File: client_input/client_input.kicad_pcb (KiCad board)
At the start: 2 copper layers, 46.5 x 47.8 mm, 26 parts, among them P1 Analog In 7-0, P2 Analog In 15-8, P4 FTDI, P5 LiPo, P6 i/o 0-7, P7 i/o 9-15, P8 i/o 15-23, P9 i/o 24-31, SW1 RST, SW2 PAIR, SW3 BTLD, U1 MCP3208, U2 MCP3208, U3 ESP-12E, U4 MCP1700-3302, U5 MCP23017, U6 MCP23017

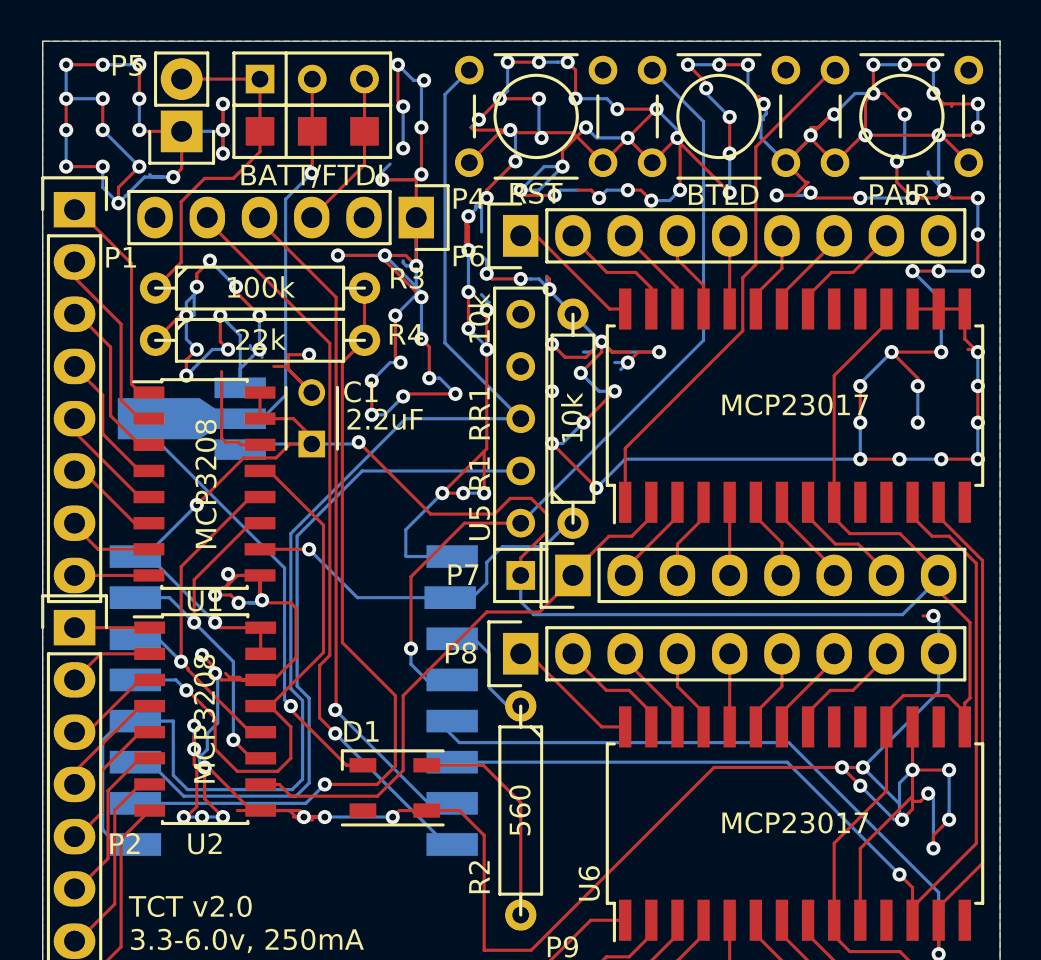
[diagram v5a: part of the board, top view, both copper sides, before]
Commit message: Nearly ready to go 2 sided. ESP + reg on back, rest on front. Stitched ground planes. Needs: some ground plane gaps filled, add some caps.
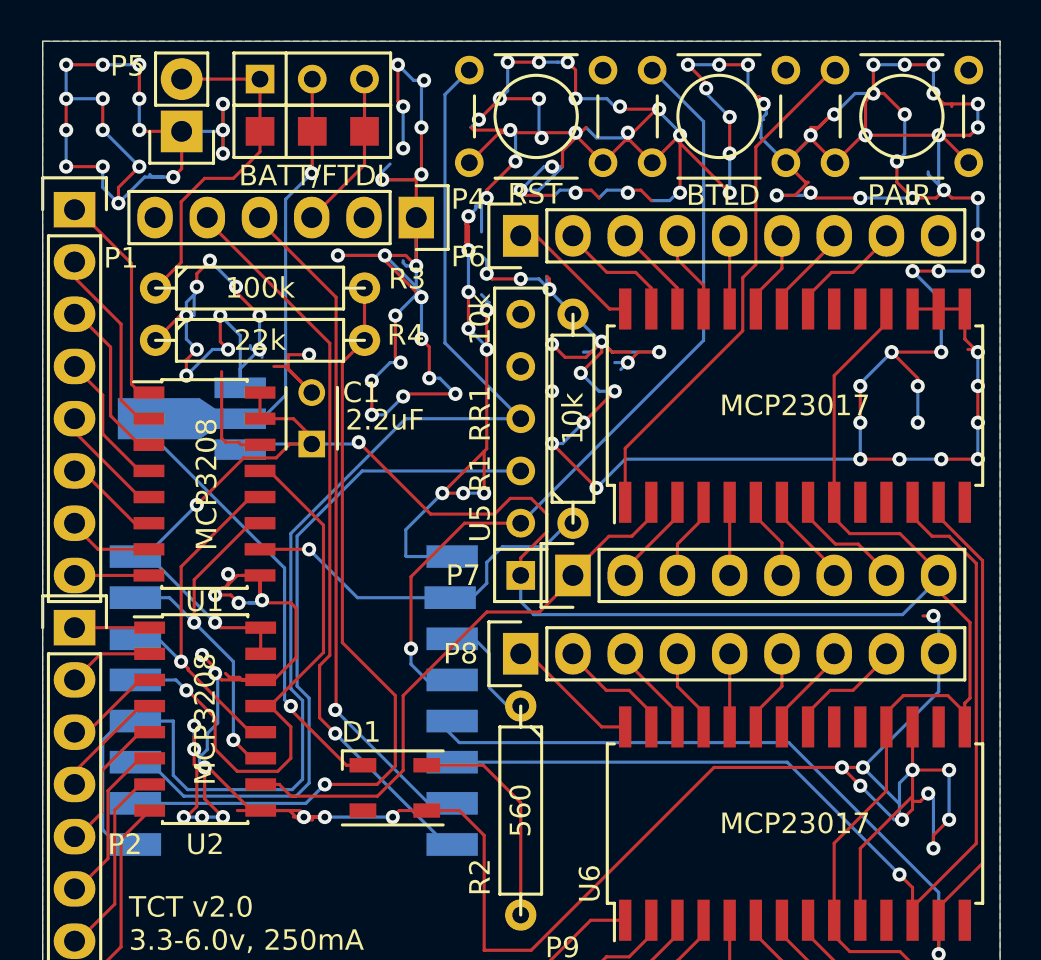
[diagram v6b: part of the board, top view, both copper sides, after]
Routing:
- net GND: vias 161 -> 159

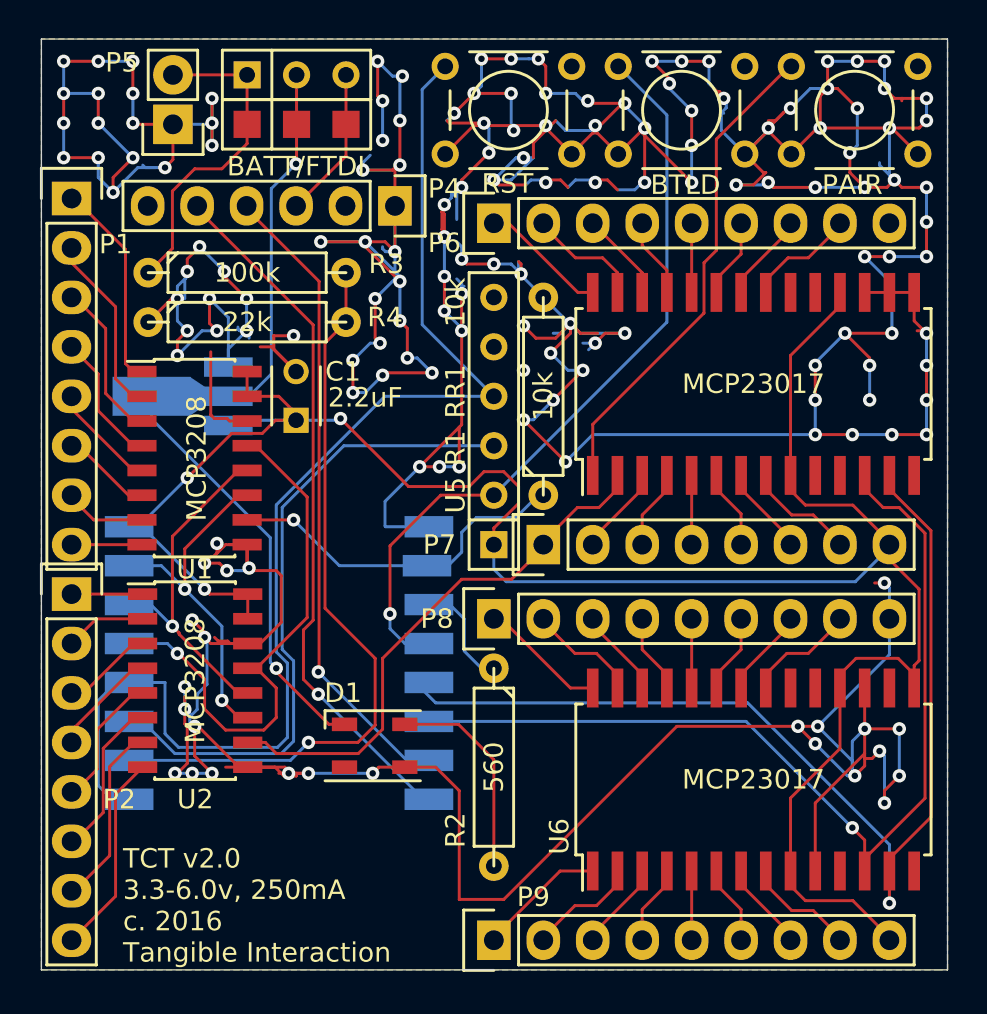
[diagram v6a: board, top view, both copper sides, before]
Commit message: improved ground planes and re-worked stitching-vias
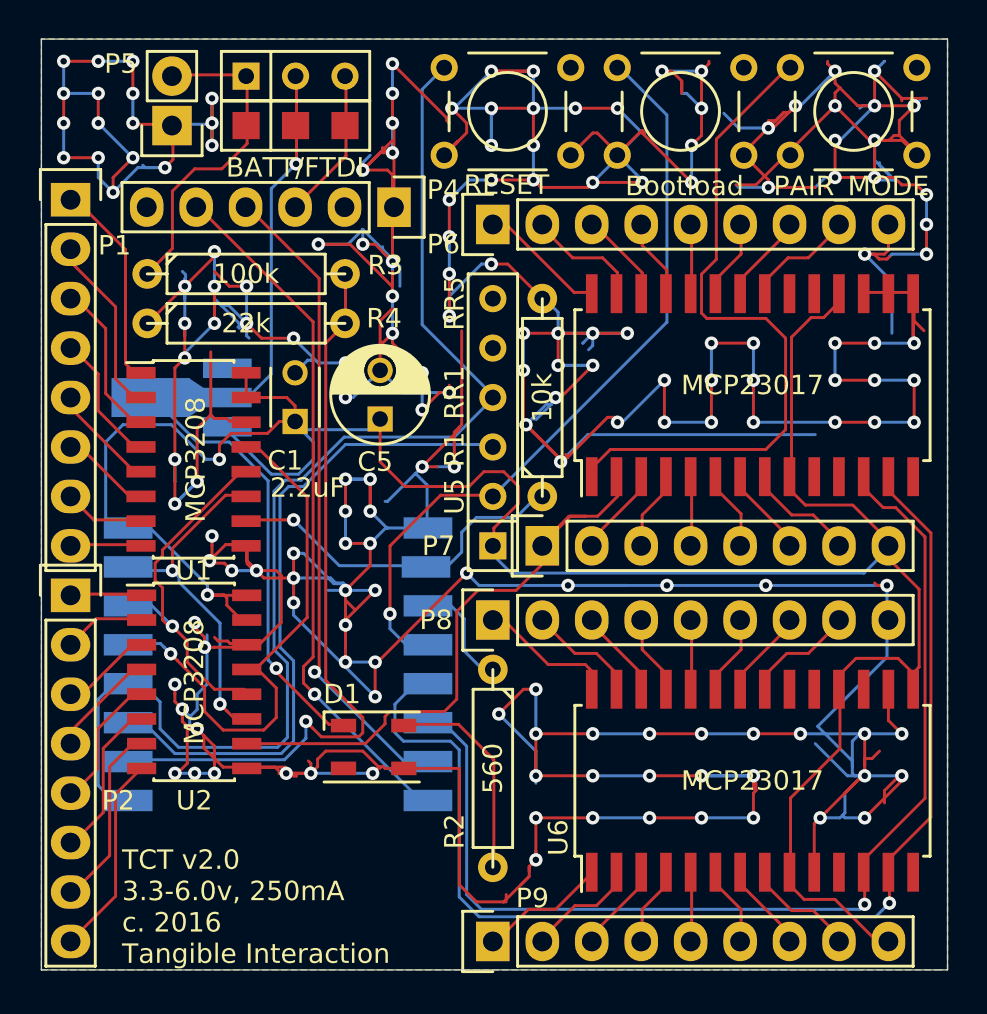
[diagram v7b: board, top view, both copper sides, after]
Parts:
- added C5: 10uF, Capacitors_ThroughHole:C_Radial_D5_L6_P2.5, F.Cu at (35.4, 34.1)
- P1: value Analog In 7-0 -> Analog In
- P2: value Analog In 15-8 -> Analog In
- P6: value i/o 0-7 -> Ribbon
- P7: value i/o 9-15 -> Ribbon
- P8: value i/o 15-23 -> Ribbon
- P9: value i/o 24-31 -> Ribbon
- RR1: value 10k -> RR5
- SW1: value RST -> RESET
- SW2: value PAIR -> PAIR_MODE
- SW3: value BTLD -> Bootload
- SW5: value (none) -> SPDT
- moved U4 0.08 mm to (25.2, 33.0)
- moved P4 0.08 mm to (36.1, 23.2)
- moved P5 0.08 mm to (24.7, 19.1)
- moved SW1 0.08 mm to (42.0, 18.3)
- moved SW2 0.08 mm to (59.8, 18.3)
- moved SW3 0.08 mm to (50.9, 18.3)
- moved P8 0.08 mm to (41.2, 44.5)
- moved R1 0.08 mm to (43.8, 33.0)
- moved ? 0.08 mm to (31.1, 19.1)
- moved R3 0.08 mm to (28.5, 26.7)
- moved R4 0.08 mm to (28.5, 29.2)
- moved SW5 0.08 mm to (31.1, 16.5)
- moved P1 0.08 mm to (19.5, 22.9)
- moved P2 0.08 mm to (19.5, 43.2)
- moved U1 0.08 mm to (25.8, 36.2)
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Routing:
- net GND: track 516.2 -> 714.6 mm, vias 159 -> 173
- net +3V3: track 116.1 -> 131.2 mm, vias 3 -> 2
- net Pair_sw: track 25.3 -> 35.3 mm
- net SCL: track 50.6 -> 57.3 mm
- net SDA: track 55.2 -> 61.5 mm
- net Net-(P7-Pad1): track 27.9 -> 31.8 mm
- net +Vin: track 44.0 -> 46.5 mm
- net MISO: track 17.2 -> 18.5 mm
- net CH_PD: track 33.1 -> 33.7 mm

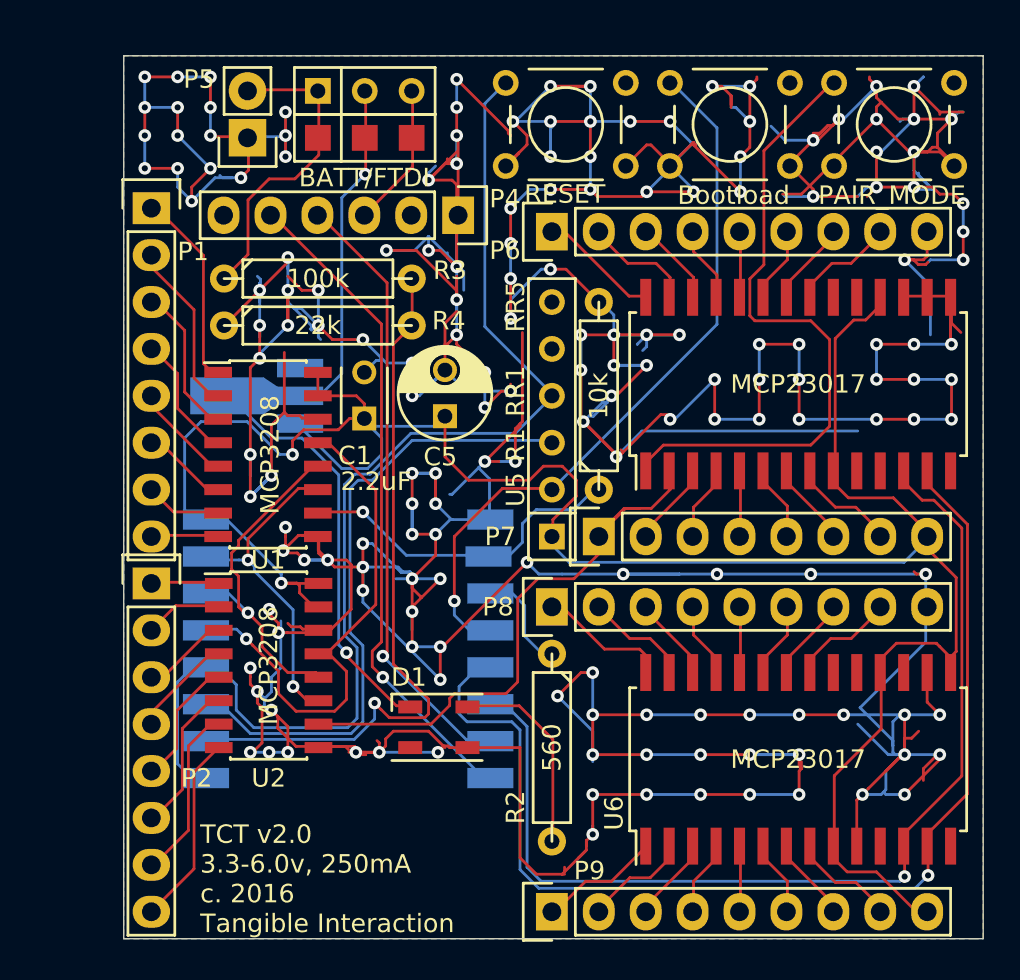
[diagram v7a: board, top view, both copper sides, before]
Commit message: Final revisions, exports, panelization, and gerbers for Rev 2. Sent to Elecrow (11 August 2016).
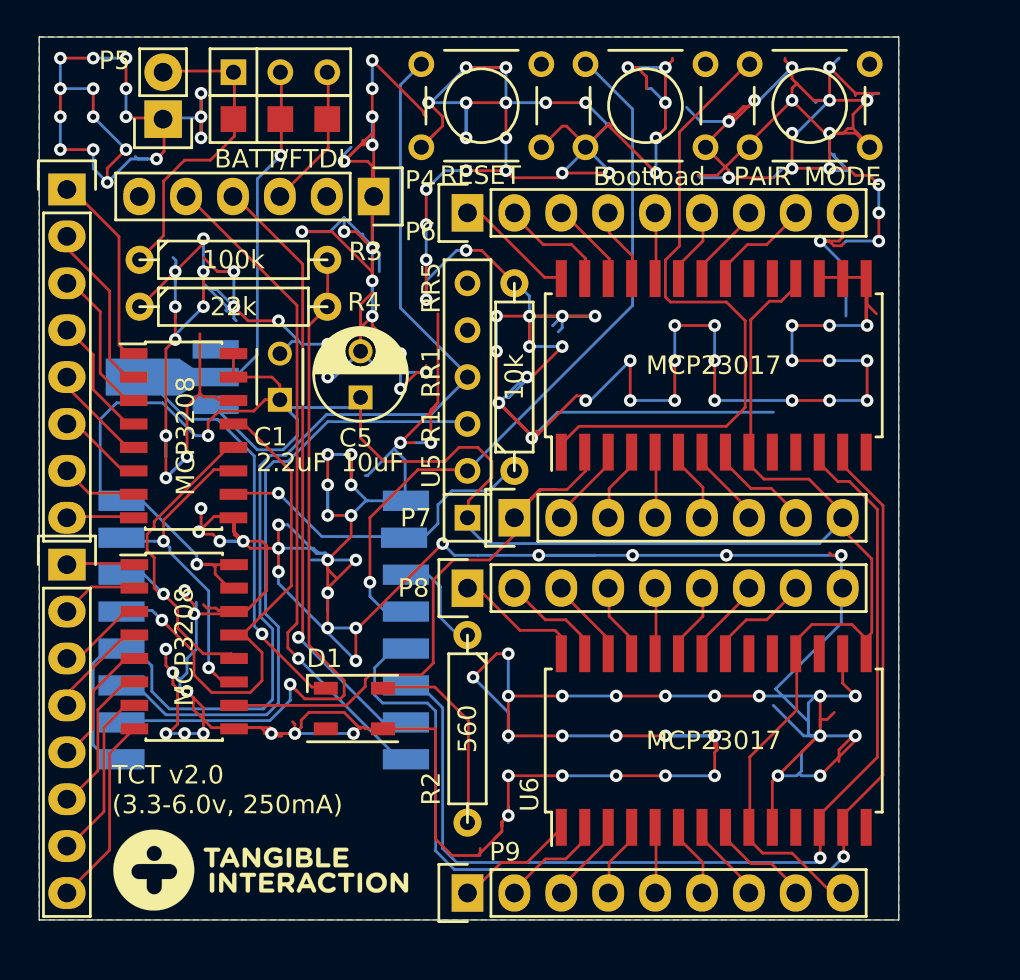
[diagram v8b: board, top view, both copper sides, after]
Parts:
- added G***: LOGO, Symbols:TI_Logo_F.SilkS_15mm, F.Cu at (25.4, 58.7)
- moved P8 4.68 mm to (36.7, 43.4)
- moved R1 4.68 mm to (39.2, 32.0)
- moved R3 4.68 mm to (24.0, 25.7)
- moved R4 4.68 mm to (24.0, 28.2)
- moved SW2 4.68 mm to (55.2, 17.3)
- moved D1 4.68 mm to (30.5, 50.0)
- moved P6 4.68 mm to (36.7, 23.1)
- moved P7 4.68 mm to (39.2, 39.6)
- moved P9 4.68 mm to (36.7, 59.9)
- moved R2 4.68 mm to (36.7, 51.1)
- moved RR1 4.68 mm to (36.7, 33.3)
- moved U4 4.68 mm to (20.7, 32.0)
- moved ? 4.68 mm to (26.5, 18.0)
- moved P5 4.68 mm to (20.2, 18.0)
- moved SW5 4.68 mm to (26.5, 15.5)
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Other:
- board text added: "TCT v2.0 (3.3-6.0v, 250mA)"
- board text removed: "TCT v2.0 3.3-6.0v, 250mA c. 2016 Tangible Interaction"
